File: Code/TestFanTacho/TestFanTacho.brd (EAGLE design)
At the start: 100 x 80 mm, 10 parts, among them IC1 317T, T1 BC548

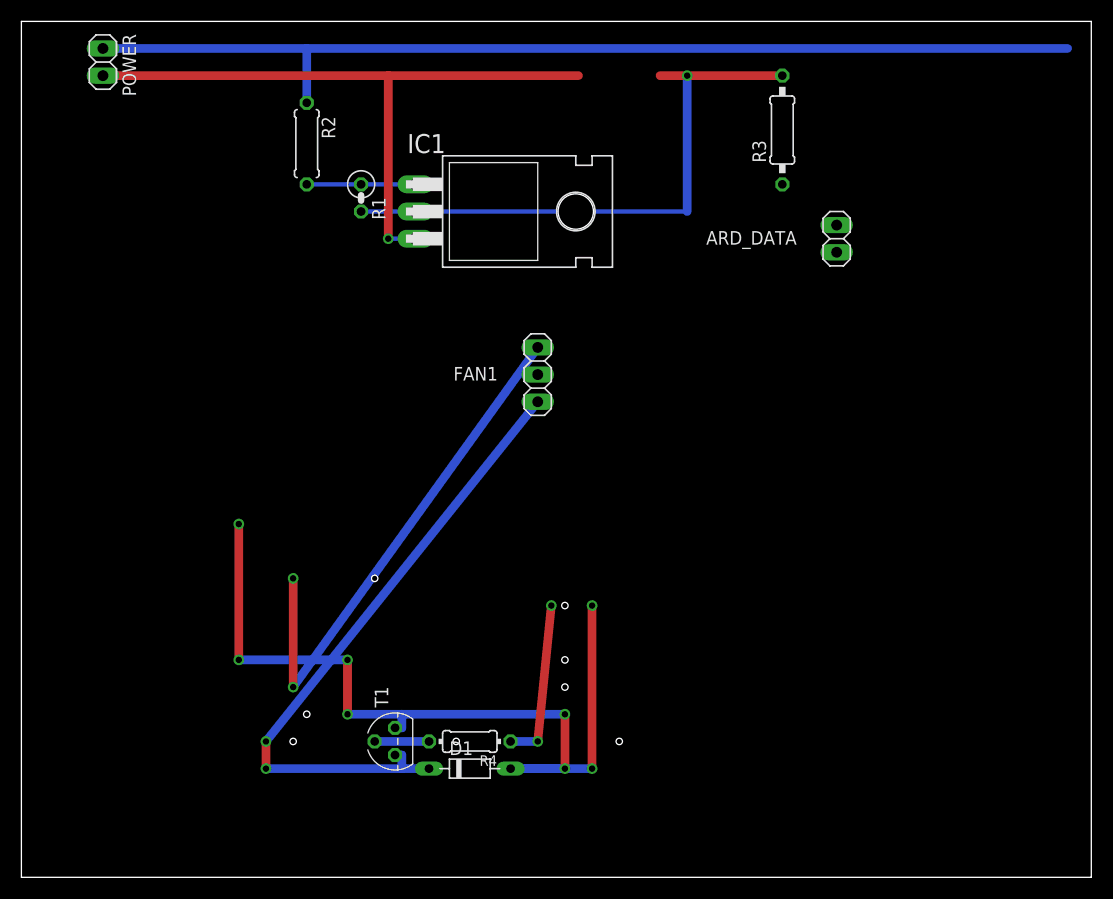
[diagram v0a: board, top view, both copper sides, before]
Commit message: Added test for the fan tacho
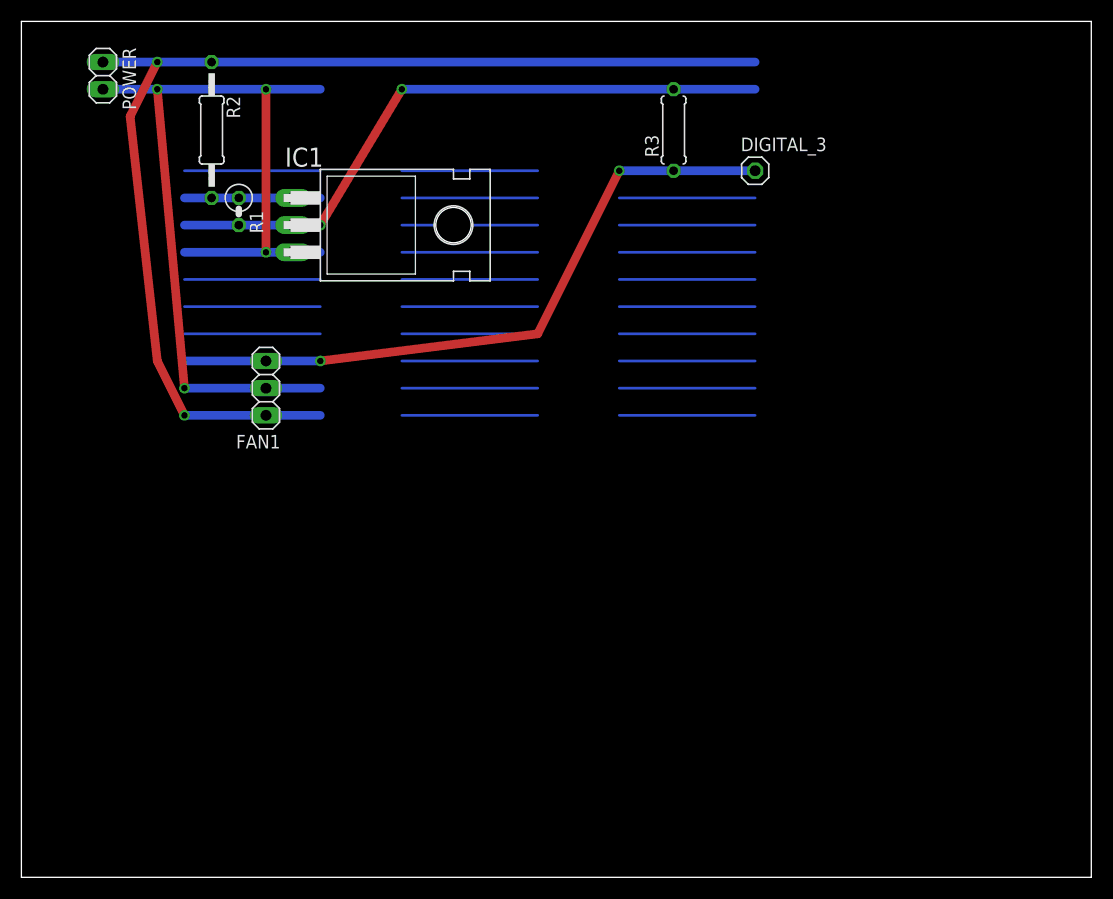
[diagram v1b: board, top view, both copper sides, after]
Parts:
- removed ARD_DATA: (no value), EnigmaMon:1X02
- removed D1: (no value), diode:D-7.5
- removed R4: 1k, rcl:0204/7
- removed T1: BC548, transistor:TO92
- added DIGITAL_3: (no value), pinhead:1X01
- R2: device EnigmaMon:0207/7 -> rcl:0207/12
- R3: device rcl:0207/10 -> rcl:0207/7
- moved FAN1 25.4 mm to (22.9, 45.7)
- moved IC1 11.5 mm to (35.6, 61.0)
- moved R1 11.5 mm to (20.3, 62.2)
- moved R3 10.2 mm to (61.0, 69.8)
- moved R2 8.98 mm to (17.8, 69.8)
- moved POWER 1.27 mm to (7.62, 74.9)
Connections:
- removed net FAN1_GND: D1.C, FAN1.3, T1.3
- removed net FAN1_PWM: ARD_DATA.1, R4.1
- removed net N$2: R4.2, T1.2
- net FAN1_TACHO: now also DIGITAL_3.1; no longer ARD_DATA.2
- net GND: now also FAN1.3; no longer D1.A, T1.1
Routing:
- net GND: track 178.4 -> 108.0 mm, vias 8 -> 2
- net N$20: track 0.00 -> 63.5 mm
- net N$15: track 0.00 -> 63.5 mm
- net FAN1_GND: track 60.3 -> 0.00 mm, vias 2 -> 0
- net +12V: track 62.2 -> 78.9 mm, vias 1 -> 4
- net FAN1_PWM: track 15.3 -> 0.00 mm, vias 2 -> 0
- net FAN1_TACHO: track 49.3 -> 62.9 mm
- net VCC: track 54.6 -> 68.2 mm, vias 1 -> 2
- net N$8: track 0.00 -> 12.7 mm
- net N$7: track 0.00 -> 12.7 mm
- net N$6: track 0.00 -> 12.7 mm
- net N$5: track 0.00 -> 12.7 mm
- net N$4: track 0.00 -> 12.7 mm
- net N$3: track 0.00 -> 12.7 mm
- net N$21: track 0.00 -> 12.7 mm
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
